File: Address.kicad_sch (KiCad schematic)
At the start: 10 parts, among them U1 74LS30, U19 74LS393, U2 74LS04, U20 74LS158, U3 74LS10, U33 74LS158, U34 74LS93, U35 74LS158

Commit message: Various corrections. Add new symbols and footprints
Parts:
- D1: footprint Diode_THT:D_DO-35_SOD27_P7.62mm_Horizontal -> K-1008:D_DO-35_SOD27_P12.70mm_Horizontal
- S1, U20, U33, U35: footprint (none) -> K-1008:DIP-16_W7.62mm_LongPads
- U1, U19, U2, U3, U34: footprint (none) -> K-1008:DIP-14_W7.62mm_LongPads
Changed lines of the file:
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@@
       (effects (font (size 1.27 1.27)))
     )
-    (property "Footprint" "" (at 125.984 145.161 0)
+    (property "Footprint" "K-1008:DIP-16_W7.62mm_LongPads" (at 125.984 145.161 0)
       (effects (font (size 1.27 1.27)) hide)
     )
@@
       (effects (font (size 1.27 1.27)))
     )
-    (property "Footprint" "" (at 45.085 48.895 0)
+    (property "Footprint" "K-1008:DIP-14_W7.62mm_LongPads" (at 45.085 48.895 0)
       (effects (font (size 1.27 1.27)) hide)
     )
@@
       (effects (font (size 1.27 1.27)))
     )
-    (property "Footprint" "" (at 104.775 66.675 0)
+    (property "Footprint" "K-1008:DIP-14_W7.62mm_LongPads" (at 104.775 66.675 0)
       (effects (font (size 1.27 1.27)) hide)
     )
@@
       (effects (font (size 1.27 1.27)))
     )
-    (property "Footprint" "" (at 125.984 109.601 0)
+    (property "Footprint" "K-1008:DIP-16_W7.62mm_LongPads" (at 125.984 109.601 0)
       (effects (font (size 1.27 1.27)) hide)
     )
@@
       (effects (font (size 1.27 1.27)))
     )
-    (property "Footprint" "" (at 65.405 28.575 0)
+    (property "Footprint" "K-1008:DIP-14_W7.62mm_LongPads" (at 65.405 28.575 0)
       (effects (font (size 1.27 1.27)) hide)
     )
@@
       (effects (font (size 1.27 1.27)))
     )
-    (property "Footprint" "Diode_THT:D_DO-35_SOD27_P7.62mm_Horizontal" (at 139.065 83.185 0)
+    (property "Footprint" "K-1008:D_DO-35_SOD27_P12.70mm_Horizontal" (at 139.065 83.185 0)
       (effects (font (size 1.27 1.27)) hide)
     )
@@
       (effects (font (size 1.27 1.27)))
     )
-    (property "Footprint" "" (at 135.255 41.275 0)
+    (property "Footprint" "K-1008:DIP-14_W7.62mm_LongPads" (at 135.255 41.275 0)
       (effects (font (size 1.27 1.27)) hide)
     )
@@
       (effects (font (size 1.27 1.27)))
     )
-    (property "Footprint" "" (at 125.984 180.721 0)
+    (property "Footprint" "K-1008:DIP-16_W7.62mm_LongPads" (at 125.984 180.721 0)
       (effects (font (size 1.27 1.27)) hide)
     )
@@
       (effects (font (size 1.27 1.27)))
     )
-    (property "Footprint" "" (at 53.975 224.155 0)
+    (property "Footprint" "K-1008:DIP-14_W7.62mm_LongPads" (at 53.975 224.155 0)
       (effects (font (size 1.27 1.27)) hide)
     )
@@
       (effects (font (size 1.27 1.27)))
     )
-    (property "Footprint" "" (at 45.085 28.575 0)
+    (property "Footprint" "K-1008:DIP-14_W7.62mm_LongPads" (at 45.085 28.575 0)
       (effects (font (size 1.27 1.27)) hide)
     )
@@
       (effects (font (size 1.27 1.27)))
     )
-    (property "Footprint" "" (at 65.405 38.735 0)
+    (property "Footprint" "K-1008:DIP-14_W7.62mm_LongPads" (at 65.405 38.735 0)
       (effects (font (size 1.27 1.27)) hide)
     )
@@
       (effects (font (size 1.27 1.27)))
     )
-    (property "Footprint" "" (at 53.975 241.935 0)
+    (property "Footprint" "K-1008:DIP-14_W7.62mm_LongPads" (at 53.975 241.935 0)
       (effects (font (size 1.27 1.27)) hide)
     )
@@
       (effects (font (size 1.27 1.27)))
     )
-    (property "Footprint" "" (at 65.405 48.895 0)
+    (property "Footprint" "K-1008:DIP-14_W7.62mm_LongPads" (at 65.405 48.895 0)
       (effects (font (size 1.27 1.27)) hide)
     )
@@
       (effects (font (size 1.27 1.27)) hide)
     )
-    (property "Footprint" "" (at 95.885 43.815 0)
+    (property "Footprint" "K-1008:DIP-16_W7.62mm_LongPads" (at 95.885 43.815 0)
       (effects (font (size 1.27 1.27)) hide)
     )
@@
       (effects (font (size 1.27 1.27)))
     )
-    (property "Footprint" "" (at 104.775 83.185 0)
+    (property "Footprint" "K-1008:DIP-14_W7.62mm_LongPads" (at 104.775 83.185 0)
       (effects (font (size 1.27 1.27)) hide)
     )
@@
     )
     (pin "1")
-    (pin "11")
-    (pin "12")
-    (pin "2")
-    (pin "3")
-    (pin "4")
-    (pin "5")
-    (pin "6")
-    (pin "8")
+    (pin "10")
+    (pin "11")
+    (pin "12")
+    (pin "13")
+    (pin "2")
+    (pin "3")
+    (pin "4")
+    (pin "5")
+    (pin "6")
+    (pin "8")
+    (pin "9")
     (pin "14")
     (pin "7")
@@
       (effects (font (size 1.27 1.27)))
     )
-    (property "Footprint" "" (at 53.975 203.835 0)
+    (property "Footprint" "K-1008:DIP-14_W7.62mm_LongPads" (at 53.975 203.835 0)
       (effects (font (size 1.27 1.27)) hide)
     )
@@
     (pin "11")
     (pin "12")
-    (pin "14")
-    (pin "2")
-    (pin "3")
+    (pin "13")
+    (pin "14")
+    (pin "2")
+    (pin "3")
+    (pin "4")
+    (pin "6")
+    (pin "7")
     (pin "8")
     (pin "9")
@@
       (effects (font (size 1.27 1.27)))
     )
-    (property "Footprint" "" (at 45.085 38.735 0)
-      (effects (font (size 1.27 1.27)) hide)
-    )
+    (property "Footprint" "K-1008:DIP-14_W7.62mm_LongPads" (at 45.085 38.735 0)
+      (effects (font (size 1.27 1.27)) hide)
+    )

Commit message: Routing completed
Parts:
- added unit 3 of U1
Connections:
- net GND: now also U34.7 (N/C)
- net KIM_A10: now also U1.9 (N/C)
- net KIM_A9: now also U1.10 (N/C)
- net at S1.4 (Pin_4), U1.2, U2.10: now also U1.13 (N/C)
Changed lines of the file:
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@@
     (comment 4 "KiCad version and corrections 2023 Eduardo Casino")
   )
+  (junction (at 64.389 88.265) (diameter 0) (color 0 0 0 0)
+  )
   (junction (at 55.245 28.575) (diameter 0) (color 0 0 0 0)
   )
@@
   (junction (at 78.105 38.735) (diameter 0) (color 0 0 0 0)
   )
+  (junction (at 66.675 90.805) (diameter 0) (color 0 0 0 0)
+  )
   (junction (at 34.925 219.075) (diameter 0) (color 0 0 0 0)
   )
+  (junction (at 78.105 66.675) (diameter 0) (color 0 0 0 0)
+  )
   (junction (at 34.925 236.855) (diameter 0) (color 0 0 0 0)
   )
@@
     (stroke (width 0) (type default))
   )
+  (wire (pts (xy 64.389 71.755) (xy 64.389 88.265))
+    (stroke (width 0) (type default))
+  )
   (wire (pts (xy 123.19 192.405) (xy 128.27 192.405))
     (stroke (width 0) (type default))
@@
     (stroke (width 0) (type default))
   )
+  (wire (pts (xy 64.389 88.265) (xy 85.09 88.265))
+    (stroke (width 0) (type default))
+  )
   (wire (pts (xy 89.535 33.655) (xy 90.805 33.655))
     (stroke (width 0) (type default))
@@
     (stroke (width 0) (type default))
   )
+  (wire (pts (xy 66.675 90.805) (xy 82.55 90.805))
+    (stroke (width 0) (type default))
+  )
   (wire (pts (xy 104.775 28.575) (xy 104.775 31.115))
     (stroke (width 0) (type default))
@@
     (stroke (width 0) (type default))
   )
-  (wire (pts (xy 31.115 88.265) (xy 85.09 88.265))
+  (wire (pts (xy 31.115 88.265) (xy 64.389 88.265))
     (stroke (width 0) (type default))
   )
@@
     (stroke (width 0) (type default))
   )
+  (wire (pts (xy 71.12 208.915) (xy 71.12 210.82))
+    (stroke (width 0) (type default))
+  )
   (wire (pts (xy 85.09 88.265) (xy 85.09 112.395))
     (stroke (width 0) (type default))
@@
     (stroke (width 0) (type default))
   )
-  (wire (pts (xy 78.105 78.105) (xy 78.105 38.735))
+  (wire (pts (xy 78.105 78.105) (xy 78.105 66.675))
     (stroke (width 0) (type default))
   )
@@
     (stroke (width 0) (type default))
   )
+  (wire (pts (xy 66.675 208.915) (xy 71.12 208.915))
+    (stroke (width 0) (type default))
+  )
+  (wire (pts (xy 66.675 69.215) (xy 66.675 90.805))
+    (stroke (width 0) (type default))
+  )
   (wire (pts (xy 66.675 201.295) (xy 95.25 201.295))
     (stroke (width 0) (type default))
@@
     (stroke (width 0) (type default))
   )
+  (wire (pts (xy 61.976 71.755) (xy 64.389 71.755))
+    (stroke (width 0) (type default))
+  )
   (wire (pts (xy 86.995 43.815) (xy 86.995 66.675))
     (stroke (width 0) (type default))
   )
-  (wire (pts (xy 31.115 90.805) (xy 82.55 90.805))
+  (wire (pts (xy 31.115 90.805) (xy 66.675 90.805))
     (stroke (width 0) (type default))
   )
@@
     (stroke (width 0) (type default))
   )
+  (wire (pts (xy 78.105 66.675) (xy 78.105 38.735))
+    (stroke (width 0) (type default))
+  )
   (wire (pts (xy 128.27 140.335) (xy 105.41 140.335))
     (stroke (width 0) (type default))
@@
     (stroke (width 0) (type default))
   )
+  (wire (pts (xy 61.976 69.215) (xy 66.675 69.215))
+    (stroke (width 0) (type default))
+  )
   (wire (pts (xy 104.775 51.435) (xy 104.775 53.975))
     (stroke (width 0) (type default))
   )
   (wire (pts (xy 67.945 236.855) (xy 66.675 236.855))
+    (stroke (width 0) (type default))
+  )
+  (wire (pts (xy 61.976 66.675) (xy 78.105 66.675))
     (stroke (width 0) (type default))
   )
@@
     )
   )
+  (symbol (lib_name "74LS30_1") (lib_id "K-1008_Library:74LS30") (at 53.34 69.215 0) (unit 3)
+    (in_bom yes) (on_board yes) (dnp no) (fields_autoplaced)
+    (property "Reference" "U1" (at 53.34 59.563 0)
+      (effects (font (size 1.27 1.27)))
+    )
+    (property "Value" "74LS30" (at 53.34 62.103 0)
+      (effects (font (size 1.27 1.27)))
+    )
+    (property "Footprint" "K-1008:DIP-14_W7.62mm_LongPads" (at 53.34 69.215 0)
+      (effects (font (size 1.27 1.27)) hide)
+    )
+    (property "Datasheet" "http://www.ti.com/lit/gpn/sn74LS30" (at 53.34 69.215 0)
+      (effects (font (size 1.27 1.27)) hide)
+    )
+    (pin "1")
+    (pin "11")
+    (pin "12")
+    (pin "2")
+    (pin "3")
+    (pin "4")
+    (pin "5")
+    (pin "6")
+    (pin "8")
+    (pin "14")
+    (pin "7")
+    (pin "10")
+    (pin "13")
+    (pin "9")
+    (instances
+      (project "k-1008-visable-memory"
+        (path "/26b75be2-cc06-4542-b320-e8a79c59fd43/4efa16a7-9de7-4861-96ca-6a92d894ba65"
+          (reference "U1") (unit 3)
+        )
+      )
+    )
+  )
   (symbol (lib_id "74xx:74LS10") (at 135.255 41.275 0) (unit 2)
     (in_bom yes) (on_board yes) (dnp no) (fields_autoplaced)
@@
         (path "/26b75be2-cc06-4542-b320-e8a79c59fd43/4efa16a7-9de7-4861-96ca-6a92d894ba65"
           (reference "U3") (unit 2)
+        )
+      )
+    )
+  )
+  (symbol (lib_id "K-1008_Library:74LS30") (at 104.775 83.185 0) (unit 1)
+    (in_bom yes) (on_board yes) (dnp no)
+    (property "Reference" "U1" (at 105.156 75.057 0)
+      (effects (font (size 1.27 1.27)))
+    )
+    (property "Value" "74LS30" (at 105.156 77.597 0)
+      (effects (font (size 1.27 1.27)))
+    )
+    (property "Footprint" "K-1008:DIP-14_W7.62mm_LongPads" (at 103.251 83.185 0)
+      (effects (font (size 1.27 1.27)) hide)
+    )
+    (property "Datasheet" "http://www.ti.com/lit/gpn/sn74LS30" (at 104.775 83.185 0)
+      (effects (font (size 1.27 1.27)) hide)
+    )
+    (pin "1")
+    (pin "11")
+    (pin "12")
+    (pin "2")
+    (pin "3")
+    (pin "4")
+    (pin "5")
+    (pin "6")
+    (pin "8")
+    (pin "14")
+    (pin "7")
+    (pin "10")
+    (pin "13")
+    (pin "9")
+    (instances
+      (project "k-1008-visable-memory"
+        (path "/26b75be2-cc06-4542-b320-e8a79c59fd43/4efa16a7-9de7-4861-96ca-6a92d894ba65"
+          (reference "U1") (unit 1)
         )
       )
@@
     )
   )
+  (symbol (lib_id "power:GND") (at 71.12 210.82 0) (unit 1)
+    (in_bom yes) (on_board yes) (dnp no)
+    (property "Reference" "#PWR01023" (at 71.12 217.17 0)
+      (effects (font (size 1.27 1.27)) hide)
+    )
+    (property "Value" "GND" (at 71.12 214.757 0)
+      (effects (font (size 1.27 1.27)))
+    )
+    (property "Footprint" "" (at 71.12 210.82 0)
+      (effects (font (size 1.27 1.27)) hide)
+    )
+    (property "Datasheet" "" (at 71.12 210.82 0)
+      (effects (font (size 1.27 1.27)) hide)
+    )
+    (pin "1")
+    (instances
+      (project "k-1008-visable-memory"
+        (path "/26b75be2-cc06-4542-b320-e8a79c59fd43/4efa16a7-9de7-4861-96ca-6a92d894ba65"
+          (reference "#PWR01023") (unit 1)
+        )
+      )
+    )
+  )
   (symbol (lib_id "power:GND") (at 127 126.365 0) (unit 1)
     (in_bom yes) (on_board yes) (dnp no)
@@
         )
       )
-    )
-  )
-  (symbol (lib_id "K-1008_Library:74LS30") (at 104.775 83.185 0) (unit 1)
-    (in_bom yes) (on_board yes) (dnp no)
-    (property "Reference" "U1" (at 106.045 74.295 0)
-      (effects (font (size 1.27 1.27)))
-    )
-    (property "Value" "74LS30" (at 106.045 76.835 0)
-      (effects (font (size 1.27 1.27)))
-    )
-    (property "Footprint" "K-1008:DIP-14_W7.62mm_LongPads" (at 104.775 83.185 0)
-      (effects (font (size 1.27 1.27)) hide)
-    )
-    (property "Datasheet" "http://www.ti.com/lit/gpn/sn74LS30" (at 104.775 83.185 0)
-      (effects (font (size 1.27 1.27)) hide)
-    )
-    (pin "1")
-    (pin "10")
-    (pin "11")
-    (pin "12")
-    (pin "13")
-    (pin "2")
-    (pin "3")
-    (pin "4")
-    (pin "5")
-    (pin "6")
-    (pin "8")
-    (pin "9")
-    (pin "14")
-    (pin "7")
-    (instances
-      (project "k-1008-visable-memory"
-        (path "/26b75be2-cc06-4542-b320-e8a79c59fd43"
-          (reference "U1") (unit 1)
-        )
-        (path "/26b75be2-cc06-4542-b320-e8a79c59fd43/4efa16a7-9de7-4861-96ca-6a92d894ba65"
-          (reference "U1") (unit 1)
-        )
-      )

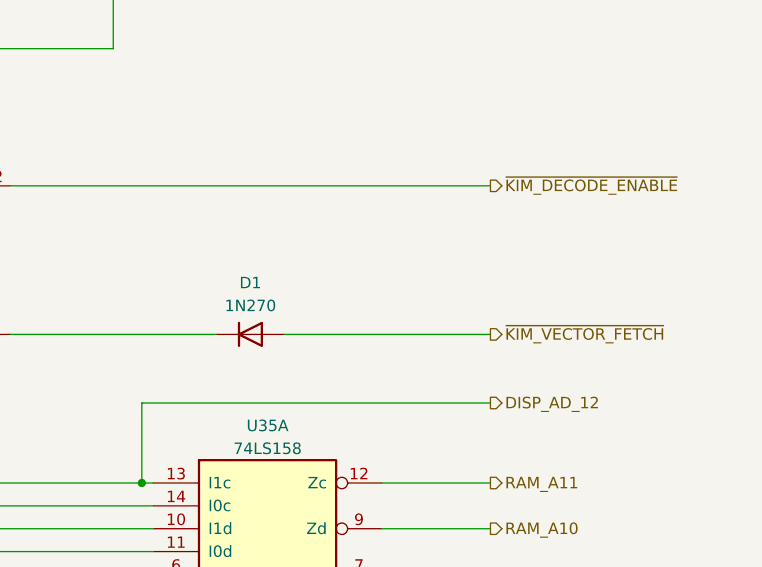
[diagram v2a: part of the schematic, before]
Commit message: Add notes for obsolete parts and replacements
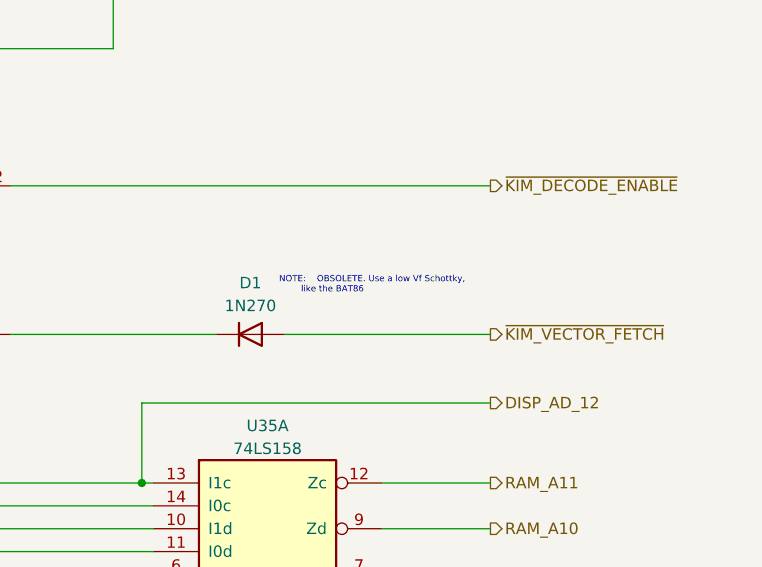
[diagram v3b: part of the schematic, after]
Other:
- note added: "NOTE: OBSOLETE. Use a low Vf Schottky, like the BAT86"
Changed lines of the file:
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@@
     (effects (font (size 1.27 1.27)) (justify left bottom))
+  )
+  (text "NOTE:	OBSOLETE. Use a low Vf Schottky,\n		like the BAT86\n"
+    (at 142.24 78.74 0)
+    (effects (font (size 0.7 0.7) (color 194 0 0 1)) (justify left bottom))
   )
   (hierarchical_label "RAM_A2" (shape output) (at 165.735 175.895 0) (fields_autoplaced)
